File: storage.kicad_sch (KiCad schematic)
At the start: 17 parts, among them J2 SD_Card, U6 W25Q128JVS

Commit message: yeah
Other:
- moved on the sheet: C36, C51
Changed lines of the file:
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@@
 	)
 	(junction
-		(at 104.14 88.9)
+		(at 104.14 87.63)
 		(diameter 0)
 		(color 0 0 0 0)
@@
 	(wire
 		(pts
-			(xy 116.84 88.9) (xy 116.84 87.63)
+			(xy 116.84 87.63) (xy 116.84 86.36)
 		)
 		(stroke
@@
 	(wire
 		(pts
-			(xy 104.14 88.9) (xy 104.14 87.63)
-		)
-		(stroke
-			(width 0)
-			(type default)
-		)
-	)
-	(wire
-		(pts
 			(xy 250.19 76.2) (xy 262.89 76.2)
 		)
@@
 	(wire
 		(pts
+			(xy 104.14 87.63) (xy 104.14 86.36)
+		)
+		(stroke
+			(width 0)
+			(type default)
+		)
+	)
+	(wire
+		(pts
 			(xy 262.89 88.9) (xy 250.19 88.9)
 		)
@@
 	(wire
 		(pts
-			(xy 104.14 88.9) (xy 116.84 88.9)
+			(xy 104.14 87.63) (xy 116.84 87.63)
 		)
 		(stroke
@@
 	(wire
 		(pts
-			(xy 116.84 77.47) (xy 116.84 80.01)
-		)
-		(stroke
-			(width 0)
-			(type default)
-		)
-	)
-	(wire
-		(pts
-			(xy 60.96 124.46) (xy 60.96 127)
+			(xy 116.84 77.47) (xy 116.84 78.74)
+		)
+		(stroke
+			(width 0)
+			(type default)
+		)
+	)
+	(wire
+		(pts
+			(xy 66.04 124.46) (xy 66.04 127)
 		)
 		(stroke
@@
 	(wire
 		(pts
-			(xy 104.14 90.17) (xy 104.14 88.9)
+			(xy 104.14 87.63) (xy 104.14 88.9)
 		)
 		(stroke
@@
 	(wire
 		(pts
-			(xy 104.14 77.47) (xy 104.14 80.01)
+			(xy 104.14 77.47) (xy 104.14 78.74)
 		)
 		(stroke
@@
 	(wire
 		(pts
-			(xy 60.96 127) (xy 71.12 127)
+			(xy 66.04 127) (xy 71.12 127)
 		)
 		(stroke
@@
 	(symbol
 		(lib_id "Device:C")
-		(at 104.14 83.82 0)
+		(at 104.14 82.55 0)
 		(unit 1)
 		(exclude_from_sim no)
@@
 		(fields_autoplaced yes)
 		(property "Reference" "C36"
-			(at 107.95 82.5499 0)
+			(at 107.95 81.2799 0)
 			(effects
 				(font
@@
 		)
 		(property "Value" "100n"
-			(at 107.95 85.0899 0)
+			(at 107.95 83.8199 0)
 			(effects
 				(font
@@
 		)
 		(property "Footprint" "0_capacitor_smd:C_0402_1005Metric"
-			(at 105.1052 87.63 0)
+			(at 105.1052 86.36 0)
 			(effects
 				(font
@@
 		)
 		(property "Datasheet" "~"
-			(at 104.14 83.82 0)
+			(at 104.14 82.55 0)
 			(effects
 				(font
@@
 		)
 		(property "Description" "Unpolarized capacitor"
-			(at 104.14 83.82 0)
+			(at 104.14 82.55 0)
 			(effects
 				(font
@@
 	(symbol
 		(lib_id "power:GND")
-		(at 104.14 90.17 0)
+		(at 104.14 88.9 0)
 		(unit 1)
 		(exclude_from_sim no)
@@
 		(fields_autoplaced yes)
 		(property "Reference" "#PWR044"
-			(at 104.14 96.52 0)
+			(at 104.14 95.25 0)
 			(effects
 				(font
@@
 		)
 		(property "Value" "GND"
-			(at 104.14 95.25 0)
+			(at 104.14 93.98 0)
 			(effects
 				(font
@@
 		)
 		(property "Footprint" ""
-			(at 104.14 90.17 0)
+			(at 104.14 88.9 0)
 			(effects
 				(font
@@
 		)
 		(property "Datasheet" ""
-			(at 104.14 90.17 0)
+			(at 104.14 88.9 0)
 			(effects
 				(font
@@
 		)
 		(property "Description" "Power symbol creates a global label with name \"GND\" , ground"
-			(at 104.14 90.17 0)
+			(at 104.14 88.9 0)
 			(effects
 				(font
@@
 	(symbol
 		(lib_id "Device:C")
-		(at 116.84 83.82 0)
+		(at 116.84 82.55 0)
 		(unit 1)
 		(exclude_from_sim no)
@@
 		(fields_autoplaced yes)
 		(property "Reference" "C51"
-			(at 120.65 82.5499 0)
+			(at 120.65 81.2799 0)
 			(effects
 				(font
@@
 		)
 		(property "Value" "1u"
-			(at 120.65 85.0899 0)
+			(at 120.65 83.8199 0)
 			(effects
 				(font
@@
 		)
 		(property "Footprint" "0_capacitor_smd:C_0603_1608Metric"
-			(at 117.8052 87.63 0)
+			(at 117.8052 86.36 0)
 			(effects
 				(font
@@
 		)
 		(property "Datasheet" "~"
-			(at 116.84 83.82 0)
+			(at 116.84 82.55 0)
 			(effects
 				(font
@@
 		)
 		(property "Description" "Unpolarized capacitor"
-			(at 116.84 83.82 0)
+			(at 116.84 82.55 0)
 			(effects
 				(font
@@
 	(symbol
 		(lib_id "power:+3.3V")
-		(at 60.96 124.46 0)
+		(at 66.04 124.46 0)
 		(unit 1)
 		(exclude_from_sim no)
@@
 		(fields_autoplaced yes)
 		(property "Reference" "#PWR045"
-			(at 60.96 128.27 0)
+			(at 66.04 128.27 0)
 			(effects
 				(font
@@
 		)
 		(property "Value" "+3V3"
-			(at 60.96 119.38 0)
+			(at 66.04 119.38 0)
 			(effects
 				(font
@@
 		)
 		(property "Footprint" ""
-			(at 60.96 124.46 0)
+			(at 66.04 124.46 0)
 			(effects
 				(font
@@
 		)
 		(property "Datasheet" ""
-			(at 60.96 124.46 0)
+			(at 66.04 124.46 0)
 			(effects
 				(font
@@
 		)
 		(property "Description" "Power symbol creates a global label with name \"+3.3V\""
-			(at 60.96 124.46 0)
-			(effects
-				(font
+			(at 66.04 124.46 0)
+			(effects
+				(font

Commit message: wen branch and pr
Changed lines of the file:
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@@
 		(company "Hoppen")
+	)
+	(bus_alias "QSPI"
+		(members "QSPI_IO0" "QSPI_IO1" "QSPI_IO2" "QSPI_IO3" "QSPI_CLK" "QSPI_nCS")
+	)
+	(bus_alias "SD"
+		(members "SD_D0" "SD_D1" "SD_D2" "SD_D3" "SD_CLK" "SD_CMD")
 	)
 	(rectangle
@@
 		)
 	)
-	(hierarchical_label "QSPI"
+	(hierarchical_label "{QSPI}"
 		(shape input)
 		(at 38.1 92.71 180)
@@
 		)
 	)
-	(hierarchical_label "SD"
+	(hierarchical_label "{SD}"
 		(shape input)
 		(at 166.37 91.44 180)

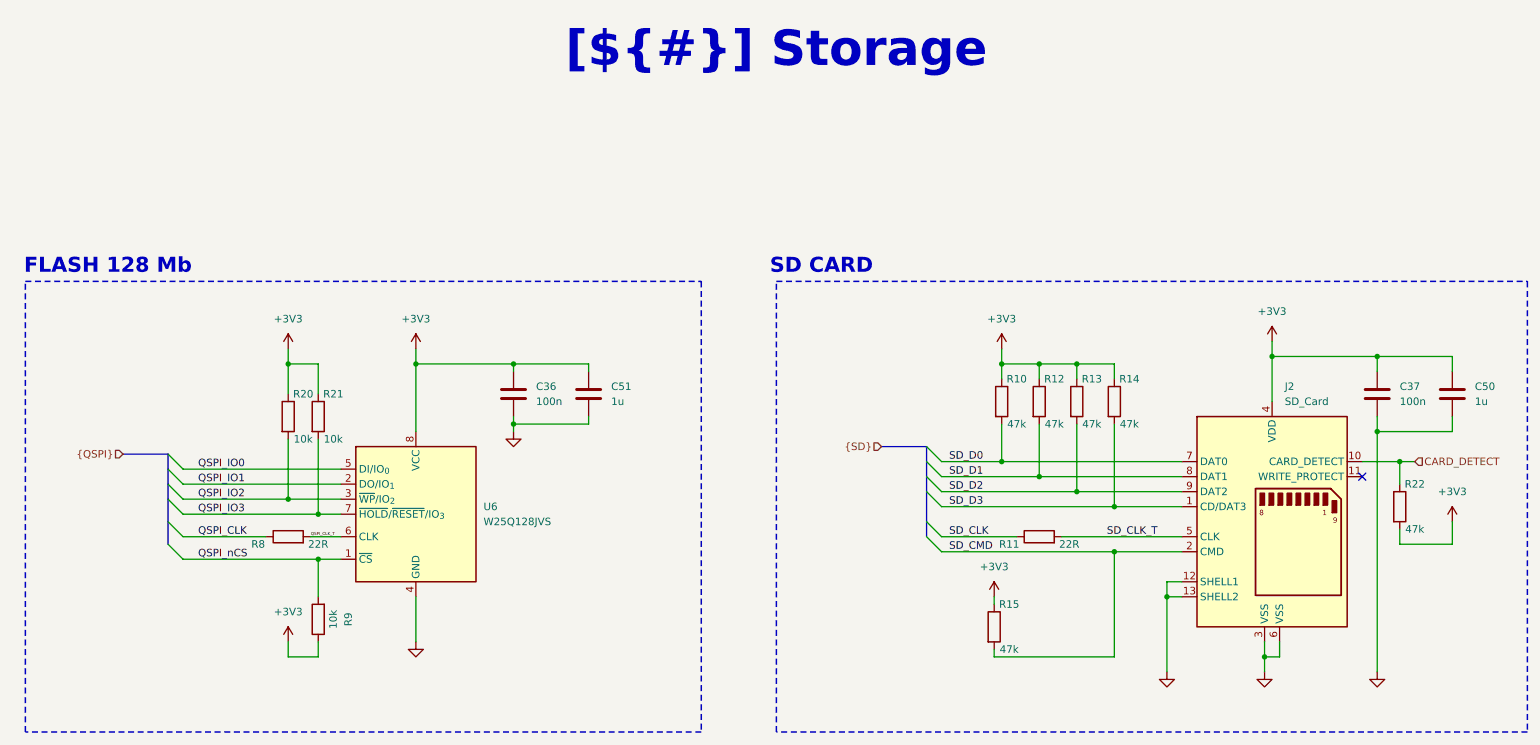
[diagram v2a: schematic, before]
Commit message: much work and .ioc file added
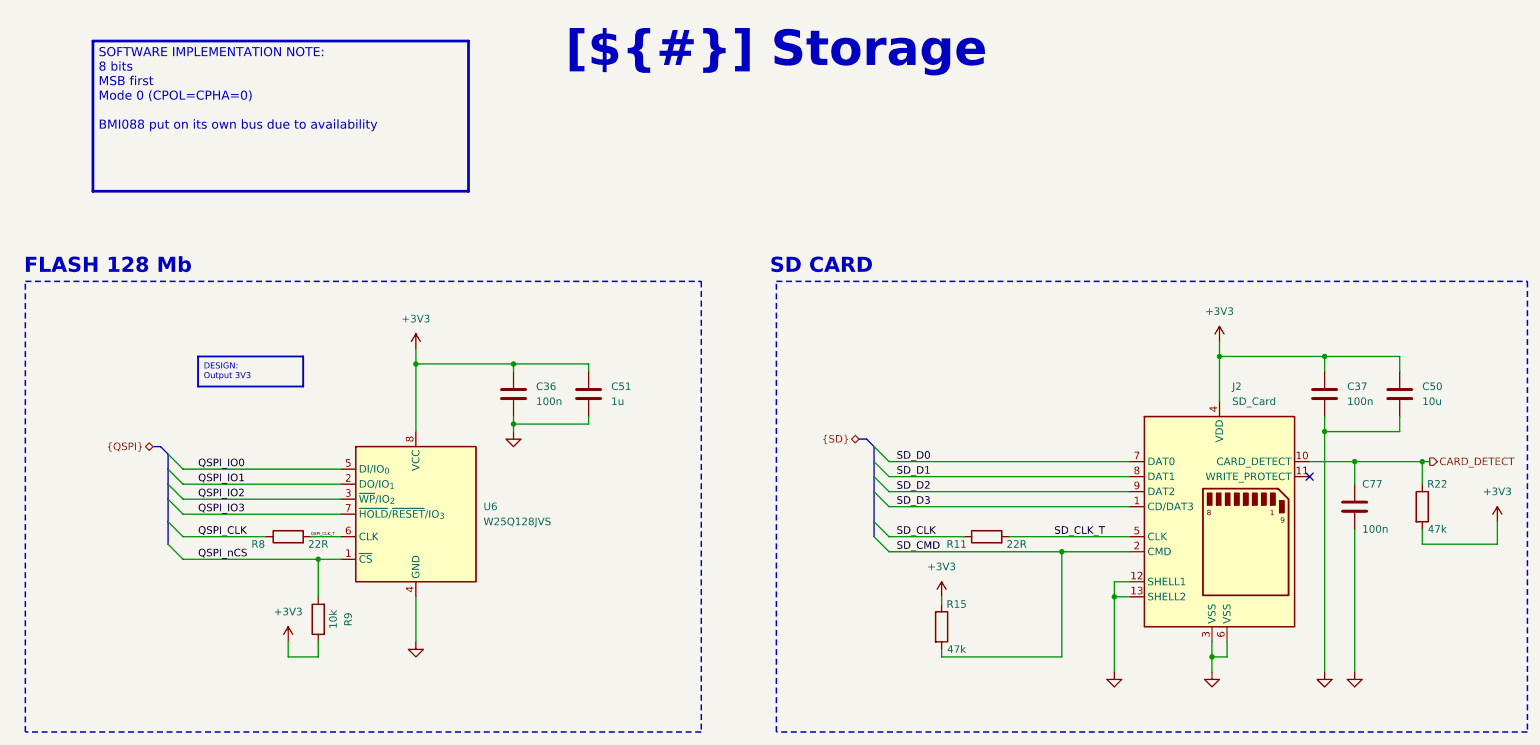
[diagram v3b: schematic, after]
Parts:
- removed R10, R12, R13, R14: 47k, 0_resistor_smd:R_0402_1005Metric, symbol Device:R
- removed R20, R21: 10k, 0_resistor_smd:R_0402_1005Metric, symbol Device:R
- added C77: 100n, 0_capacitor_smd:C_0402_1005Metric, symbol Device:C
- C50: value 1u -> 10u
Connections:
- net CARD_DETECT: now also C77.1
- net GND: now also C77.2
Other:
- moved on the sheet: C37, C50, J2, R11, R15, R22

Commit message: start fix fp
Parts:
- removed C77: 100n, 0_capacitor_smd:C_0402_1005Metric, symbol Device:C
- removed J2: SD_Card, symbol 0_storage:SD_Card_Receptacle
- removed R15, R22: 47k, 0_resistor_smd:R_0402_1005Metric, symbol Device:R
- added J19: MicroSD Card Holder, 0_storage:microSD_HC_Hirose_DM3D-SF, symbol 0_storage:Micro_SD_Card_Det1
- added R10: 22R, 0_resistor_smd:R_0402_1005Metric, symbol Device:R
- added R12: 10k, 0_resistor_smd:R_0402_1005Metric, symbol Device:R
- C50: value 10u -> 1u
- R11: value 22R -> 10k
- U6: footprint Package_SO:SOIC-8_5.3x5.3mm_P1.27mm -> 0_storage:SOIC-8_5.3x5.3mm_P1.27mm; LCSC (none) -> C97521
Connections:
- net SD_CLK_T is gone; now on net SD_CMD: R11.2
- net +3V3: now also C37.2, C50.2, R11.1, R9.2, J19.4 (VDD), R12.2; no longer C37.1, C50.1, R9.1
- net CARD_DETECT: now also J19.10 (A), R12.1
- net GND: now also C37.1, C50.1, J19.11 (SHIELD), J19.6 (VSS), J19.9 (B); no longer C37.2, C50.2
- net QSPI_nCS: now also R9.1; no longer R9.2
- net SD_CLK: now also R10.1; no longer R11.1
- net SD_CMD: now also J19.3 (CMD)
- net SD_D0: now also J19.7 (DAT0)
- net SD_D1: now also J19.8 (DAT1)
- net SD_D2: now also J19.1 (DAT2)
- net SD_D3: now also J19.2 (DAT3/CD)
- new net: J19.5 (CLK), R10.2
- no-connect marks 1 -> 0
